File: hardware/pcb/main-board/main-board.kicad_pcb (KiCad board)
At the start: 2 copper layers, 100 x 80 mm, 44 parts, among them J1 USB-C, J10 CH552G_KEYBOARD_MCU, J11 KEYBOARD_BACKLIGHT_LEDS, J12 SPEAKER_1W_8OHM, J2 BATT_2x18650_PARALLEL, J3 BOOT0_OVERRIDE_JUMPER, J4 SWD_DEBUG, J5 MICROSD, J6 CR2032_HOLDER, J7 U.FL, J8 SMA_EDGE, J9 RA8875_DISPLAY_MODULE, Q1 2N7002, SW1 PWR_KEY, SW2 RESET, U1 MCP73831-2-OT, U10 PAM8403D, U2 IP5306, U3 AMS1117-3.3, U4 AMS1117-3.3, U5 GD32VF103CCT6, U6 W25Q64JVSSIQ, U7 23LC1024, U8 DS3231M, U9 ESP32-C3-MINI-1U, Y1 8MHz

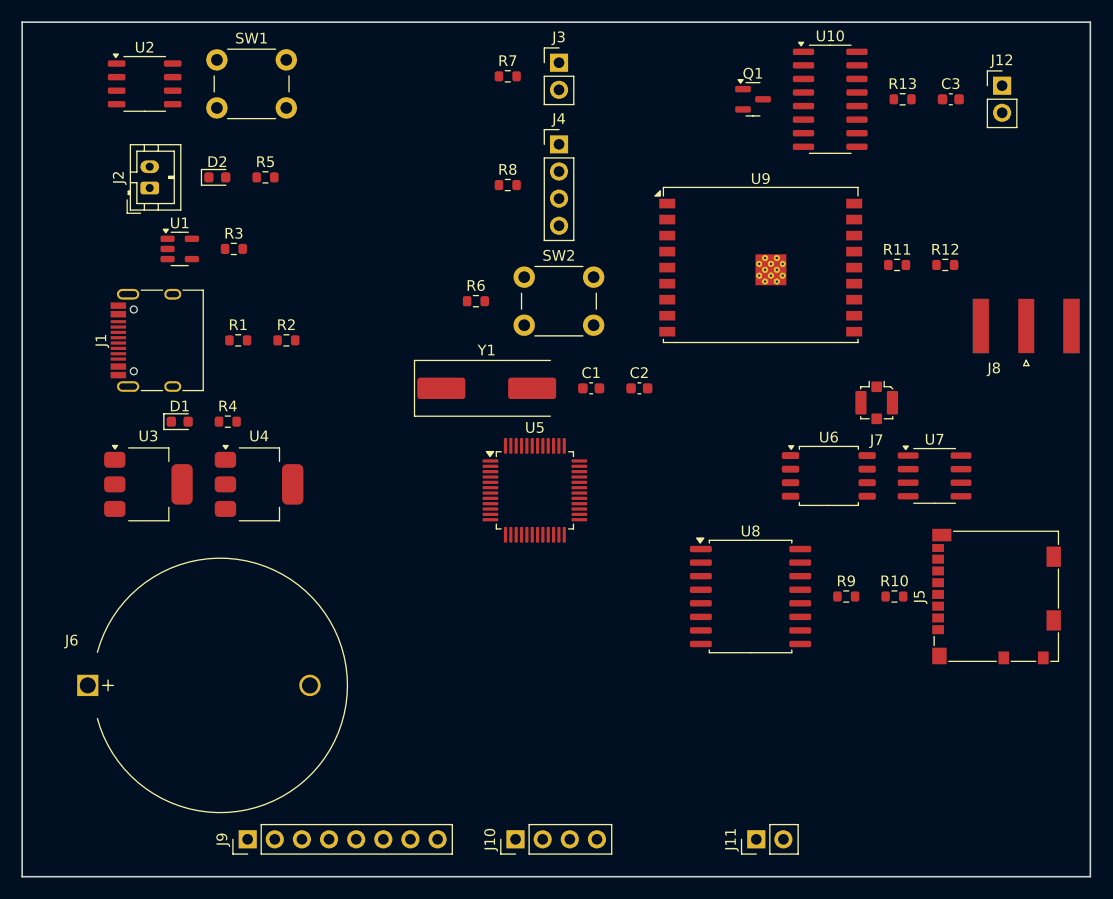
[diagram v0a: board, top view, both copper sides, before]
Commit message: hardware: route the Main Board PCB with Freerouting
Routes main-board.kicad_pcb (was placement-only) via Freerouting 2.2.4,
run headless through its CLI -- no GUI, no manual click-routing. Neither
Freerouting nor a Java runtime new enough to run it (it needs Java 25;
the environment had 21) were available, so both were fetched for this
pass.

170 of 171 connections auto-routed across 2 layers (F.Cu/B.Cu) in 10
passes (~31s). One net (/DISP_CS, MCU to the display header) is left
unrouted -- it sits in a congested area the autorouter couldn't clear
even at 30 passes, and finishing that one trace by hand in KiCad's PCB
editor is the realistic path forward, not more autorouter time.

kicad-cli pcb drc: 12 violations, all the same pre-existing
drill_out_of_range on U9's placeholder footprint (see prior commit) --
courtyard/shorting/clearance all clean.

Co-Authored-By: Claude Sonnet 5 <noreply@anthropic.com>
Claude-Session: https://claude.ai/code/session_01Qv22nN2Gzvn3yFBup6Askg
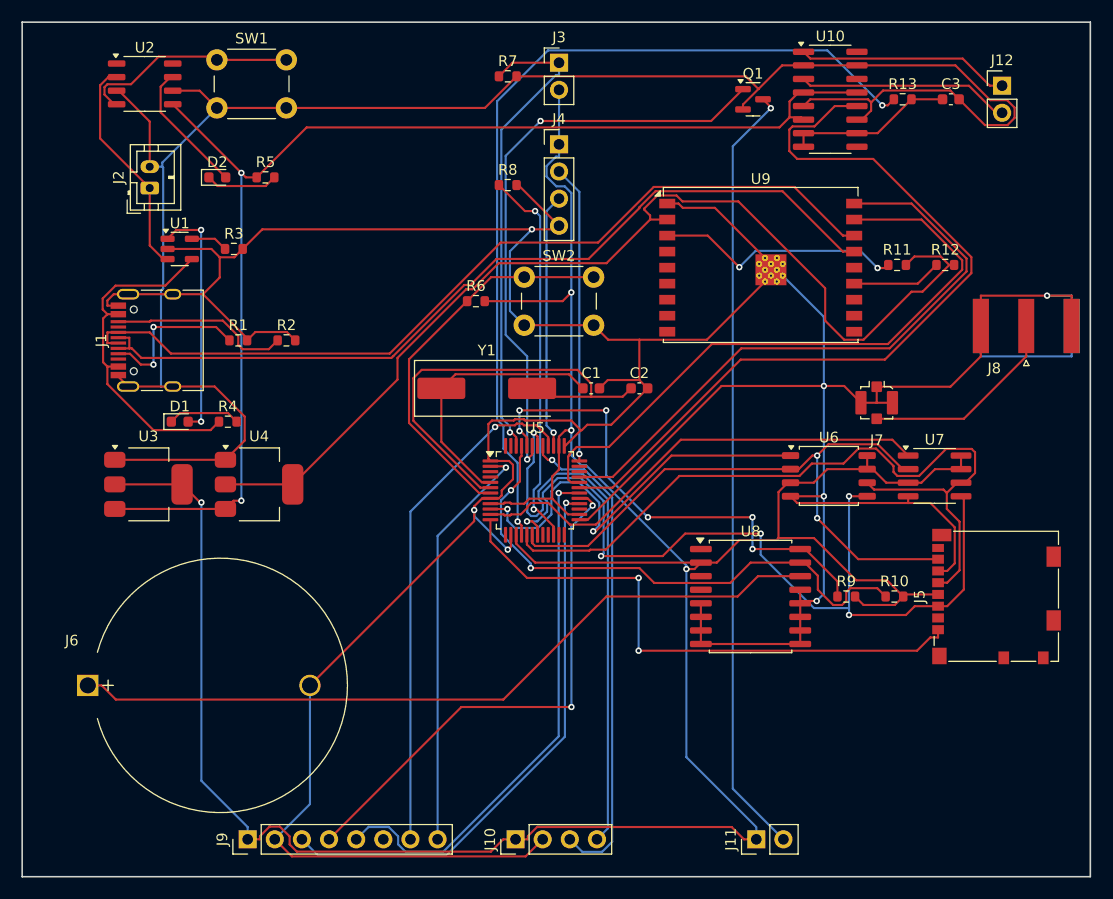
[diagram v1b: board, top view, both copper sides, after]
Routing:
- net GND: track 0.00 -> 582.2 mm, vias 0 -> 7
- net /+3V3_MCU: track 0.00 -> 275.2 mm, vias 0 -> 4
- net +5V: track 0.00 -> 115.3 mm, vias 0 -> 2
- net /+3V3_RF: track 0.00 -> 98.6 mm
- net /AUDIO_PWM: track 0.00 -> 83.0 mm, vias 0 -> 2
- net /USB_DP: track 0.00 -> 81.1 mm
- net /USB_DN: track 0.00 -> 80.1 mm
- net /SPI1_MOSI: track 0.00 -> 80.1 mm, vias 0 -> 5
- net /AUDIO_SHDN: track 0.00 -> 76.9 mm
- net /SPI1_SCK: track 0.00 -> 73.1 mm
- net /KBL_DRAIN: track 0.00 -> 73.0 mm, vias 0 -> 1
- net /VBAT_RTC: track 0.00 -> 72.0 mm
- net /USART1_TX: track 0.00 -> 60.1 mm
- net /SPI1_MISO: track 0.00 -> 59.8 mm, vias 0 -> 2
- net /USART1_RX: track 0.00 -> 58.1 mm
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
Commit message: hardware: regenerate the Main Board PCB against the corrected netlist
The previous PCB was routed against the pre-datasheet-fix netlist, so
its net-to-pad assignments on the MCU, ESP32-C3 module, and IP5306
were wrong, not just stale. Regenerated from scratch: fresh netlist
export, fresh placement (build_pcb.py), fresh Freerouting pass.

Freerouting completed 170 of 171 nets; the one holdout was /USB_DN
(J1's two D- pins, 1mm apart with /USB_DP's pad physically between
them) rather than /DISP_CS this time -- /DISP_CS routed cleanly once
it was routing the pad that's actually /DISP_CS now (pad 25, not the
old netlist's pad 27). Finished /USB_DN by hand: the west side of the
connector was already fully claimed by /USB_DP, VBUS, and /CHG_STAT
with no spare lane, so it routes east instead, into open board area.

Result: 171/171 routed, DRC clean except the pre-existing
drill_out_of_range warnings on U9's WROOM-02U placeholder footprint
(unrelated, already documented).

Co-Authored-By: Claude Sonnet 5 <noreply@anthropic.com>
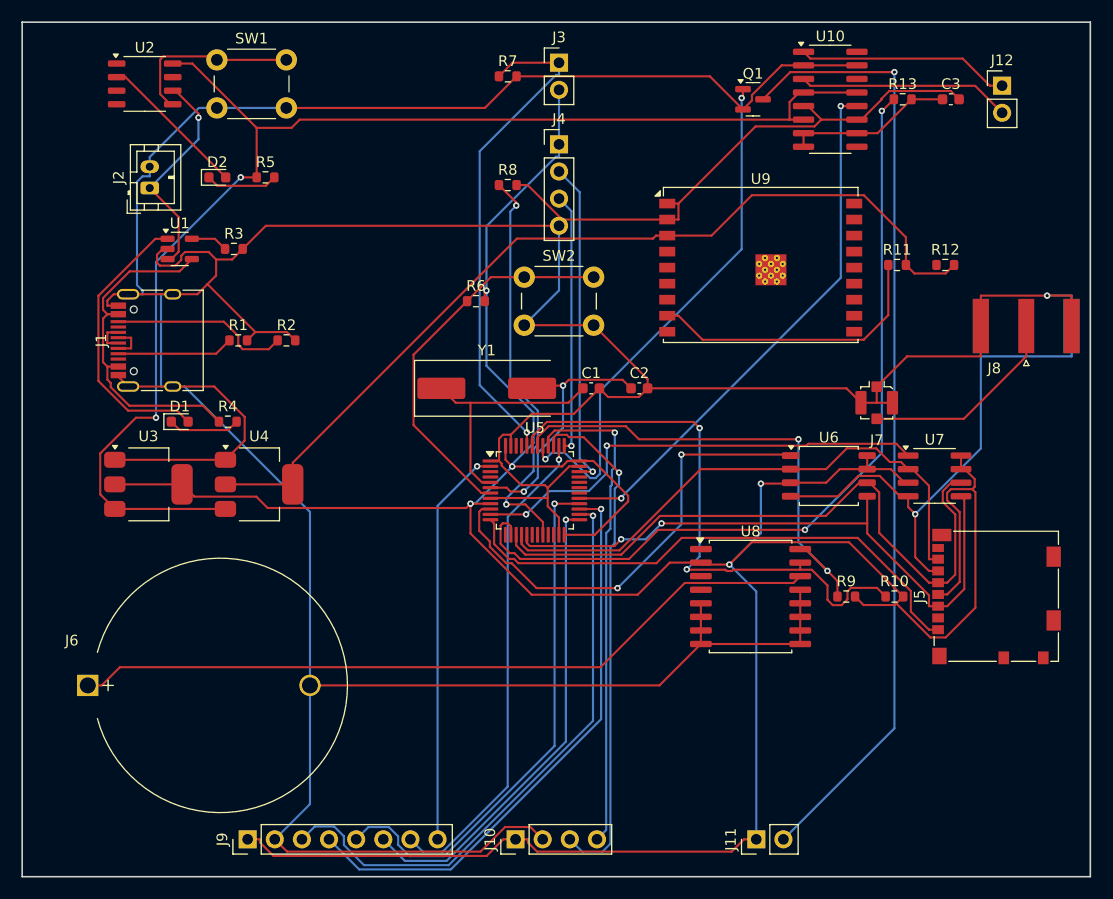
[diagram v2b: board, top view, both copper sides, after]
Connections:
- U2 pad 2: /VBATT -> /BATT_LED1
- U2 pad 3: GND -> unconnected-(U2-LED2-Pad3)
- U2 pad 4: /PWR_KEY -> unconnected-(U2-LED3-Pad4)
- U2 pad 5: +5V -> /PWR_KEY
- U2 pad 6: GND -> /VBATT
- U2 pad 7: /BATT_LED1 -> unconnected-(U2-SW-Pad7)
- U2 pad 8: unconnected-(U2-LED2-Pad8) -> +5V
- U5 pad 14: GND -> /AUDIO_PWM
- U5 pad 15: /+3V3_MCU -> /SPI1_SCK
- U5 pad 16: /AUDIO_PWM -> /SPI1_MISO
- U5 pad 17: /SPI1_SCK -> /SPI1_MOSI
- U5 pad 18: /SPI1_MISO -> unconnected-(U5-PB0-Pad18)
- U5 pad 19: /SPI1_MOSI -> unconnected-(U5-PB1-Pad19)
- U5 pad 20: unconnected-(U5-PB0-Pad20) -> /BOOT1
- U5 pad 22: /BOOT1 -> unconnected-(U5-PB11-Pad22)
- U5 pad 23: unconnected-(U5-PB10-Pad23) -> GND
- U5 pad 24: unconnected-(U5-PB11-Pad24) -> /+3V3_MCU
- U5 pad 25: GND -> /DISP_CS
- U5 pad 26: /+3V3_MCU -> /SPI2_SCK
- U5 pad 27: /DISP_CS -> /SPI2_MISO
- U5 pad 28: /SPI2_SCK -> /SPI2_MOSI
- U5 pad 29: /SPI2_MISO -> /AUDIO_SHDN
- U5 pad 30: /SPI2_MOSI -> /USART1_TX
- U5 pad 31: /AUDIO_SHDN -> /USART1_RX
- U5 pad 32: /USART1_TX -> unconnected-(U5-PA11-Pad32)
- U5 pad 33: /USART1_RX -> unconnected-(U5-PA12-Pad33)
- U5 pad 34: unconnected-(U5-PA11-Pad34) -> /SWDIO
- U5 pad 35: unconnected-(U5-PA12-Pad35) -> GND
- U5 pad 36: /SWDIO -> /+3V3_MCU
- U5 pad 37: GND -> /SWCLK
- U5 pad 38: /+3V3_MCU -> /DISP_RESET
- U5 pad 39: /SWCLK -> /USART2_TX
- U5 pad 40: /DISP_RESET -> /USART2_RX
- U5 pad 41: /USART2_TX -> /KBD_BACKLIGHT_PWM
- U5 pad 42: /USART2_RX -> /I2C1_SCL
- U5 pad 43: /KBD_BACKLIGHT_PWM -> /I2C1_SDA
- U5 pad 44: /I2C1_SCL -> /BOOT0
- U5 pad 45: /I2C1_SDA -> unconnected-(U5-PB8-Pad45)
- U5 pad 46: /BOOT0 -> unconnected-(U5-PB9-Pad46)
- U5 pad 47: unconnected-(U5-PB8-Pad47) -> GND
- U5 pad 48: unconnected-(U5-PB9-Pad48) -> /+3V3_MCU
- U9 pad 10: unconnected-(U9-IO6-Pad10) -> (no net)
- U9 pad 11: unconnected-(U9-IO7-Pad11) -> (no net)
- U9 pad 13: /ESP_IO9 -> unconnected-(U9-IO1-Pad13)
- U9 pad 14: unconnected-(U9-IO10-Pad14) -> (no net)
- U9 pad 15: /USB_DN -> (no net)
- U9 pad 16: /USB_DP -> unconnected-(U9-IO10-Pad16)
- U9 pad 17: /USART1_TX -> (no net)
- U9 pad 18: /USART1_RX -> unconnected-(U9-IO4-Pad18)
- U9 pad 19: GND -> unconnected-(U9-IO5-Pad19)
- U9 pad 2: /+3V3_RF -> GND
- U9 pad 3: /ESP_EN -> /+3V3_RF
- U9 pad 4: unconnected-(U9-IO0/BOOT_SEL-Pad4) -> (no net)
- U9 pad 7: unconnected-(U9-IO3-Pad7) -> (no net)
- U9 pad 8: unconnected-(U9-IO4-Pad8) -> /ESP_EN
- U9 pad 9: unconnected-(U9-IO5-Pad9) -> (no net)
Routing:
- net /USB_DP: track 81.1 -> 3.05 mm
- net /USB_DN: track 80.1 -> 3.39 mm
- net /USART1_TX: track 60.1 -> 0.00 mm
- net /USART1_RX: track 58.1 -> 0.00 mm
- net /DISP_CS: track 0.00 -> 44.6 mm, vias 0 -> 1
- net /+3V3_MCU: track 275.2 -> 301.9 mm, vias 4 -> 5
- net /AUDIO_SHDN: track 76.9 -> 50.7 mm, vias 0 -> 2
- net GND: track 582.2 -> 557.4 mm, vias 7 -> 2
- net /SPI1_MOSI: track 80.1 -> 59.1 mm, vias 5 -> 2
- net /OSC_OUT: track 42.4 -> 24.7 mm, vias 0 -> 2
- net /KBL_DRAIN: track 73.0 -> 89.5 mm
- net /+3V3_RF: track 98.6 -> 85.5 mm
- net /SPI1_SCK: track 73.1 -> 62.0 mm
- net unconnected-(U9-IO5-Pad19): track 0.00 -> 11.0 mm
- net +5V: track 115.3 -> 124.8 mm
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
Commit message: hardware: add the IP5306's missing boost inductor
Datasheet verification (previous commit) found the IP5306's SW pin
(the boost converter's switch node) was wired to nothing -- the boost
path (BAT -> VOUT) couldn't function without an inductor there, and
none existed anywhere in this design.

Fixed per the IP5306 datasheet's own "Typical Application Schematic"
(Figure 7): a 1uH inductor (L1) bridges SW to BAT directly, not to
VOUT as an earlier read of this design assumed -- it's shared between
the buck charger and boost discharger. Added the reference circuit's
RC snubber (R14 0.5R + C4 22uF) on the SW node and a VOUT decoupling
cap (C5, simplified from the datasheet's 4-cap bank to one).

Regenerated the schematic (ERC clean) and the PCB from scratch against
the updated netlist: fresh placement (the new parts go in the open
board area below the MCU cluster, since the CR2032 holder's real
courtyard already fills the power-tree column), fresh Freerouting
pass, one net (/USB_DN, unrelated -- same fix as the previous PCB
regeneration) finished by hand. All 87 nets routed, DRC clean except
the pre-existing, already-documented ESP32 placeholder footprint
warning.

Flagged for the next design-review pass: the new SW/inductor path
carries boost-converter current (up to 2.4A) but was auto-routed at
the board's default 0.2mm trace width, which is undersized for it.

Co-Authored-By: Claude Sonnet 5 <noreply@anthropic.com>
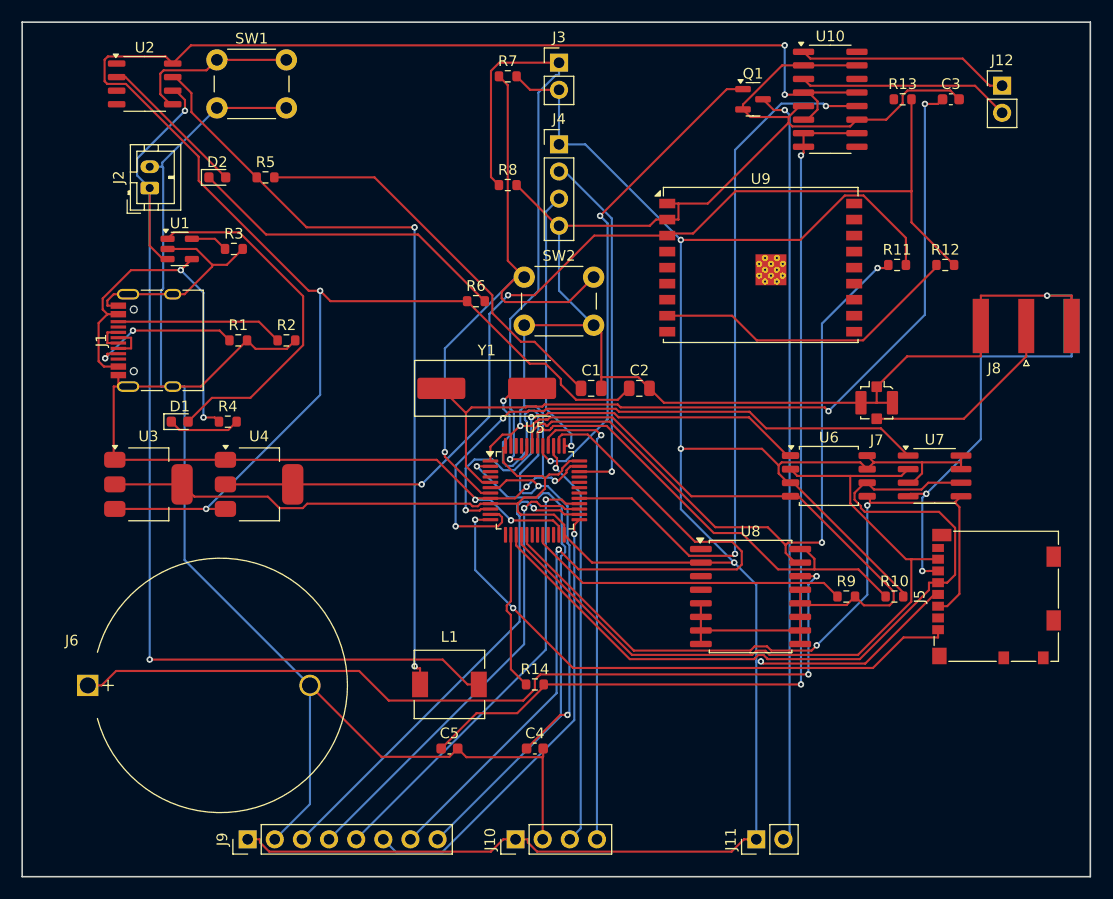
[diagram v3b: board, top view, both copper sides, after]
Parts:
- added C4: 20pF, C_0603_1608Metric, F.Cu at (48.0, 68.0)
- added C5: 100nF, C_0603_1608Metric, F.Cu at (40.0, 68.0)
- added L1: 1uH, L_6.3x6.3_H3, F.Cu at (40.0, 62.0)
- added R14: 1k, R_0603_1608Metric, F.Cu at (48.0, 62.0)
- C1, C2: value 20pF -> 22uF; footprint C_0603_1608Metric -> C_0805_2012Metric
- C3: value 100nF -> 20pF
- R11: value 10k -> 4.7k
- R13: value 1k -> 10k
- R5: value 1k -> 0.5R
- R6: value 10k -> 1k
- R9: value 4.7k -> 10k
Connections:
- C1 pad 1: /OSC_IN -> /SNUBBER_MID
- C2 pad 1: /OSC_OUT -> +5V
- C3 pad 1: /AUDIO_IN -> /OSC_IN
- R10 pad 1: /I2C1_SDA -> /I2C1_SCL
- R11 pad 1: /ESP_EN -> /I2C1_SDA
- R11 pad 2: /+3V3_RF -> /+3V3_MCU
- R12 pad 1: /ESP_IO9 -> /ESP_EN
- R13 pad 1: /AUDIO_PWM -> /ESP_IO9
- R13 pad 2: /AUDIO_IN -> /+3V3_RF
- R5 pad 1: +5V -> /IP5306_SW
- R5 pad 2: /BATT_LED1_R -> /SNUBBER_MID
- R6 pad 1: /NRST -> +5V
- R6 pad 2: /+3V3_MCU -> /BATT_LED1_R
- R7 pad 1: /BOOT0 -> /NRST
- R7 pad 2: GND -> /+3V3_MCU
- R8 pad 1: /BOOT1 -> /BOOT0
- R9 pad 1: /I2C1_SCL -> /BOOT1
- R9 pad 2: /+3V3_MCU -> GND
- U2 pad 7: unconnected-(U2-SW-Pad7) -> /IP5306_SW
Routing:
- net /AUDIO_IN: track 15.6 -> 93.0 mm, vias 0 -> 2
- net /VBATT: track 20.6 -> 95.6 mm, vias 1 -> 2
- net /IP5306_SW: track 0.00 -> 72.7 mm, vias 0 -> 2
- net /AUDIO_PWM: track 77.7 -> 14.9 mm, vias 2 -> 0
- net /OSC_IN: track 23.1 -> 80.0 mm, vias 0 -> 2
- net +5V: track 124.8 -> 181.2 mm, vias 2 -> 4
- net GND: track 557.4 -> 517.8 mm, vias 2 -> 8
- net /SNUBBER_MID: track 0.00 -> 37.9 mm
- net /OSC_OUT: track 24.7 -> 60.7 mm, vias 2 -> 3
- net /DISP_RESET: track 46.0 -> 74.8 mm
- net /BATT_LED1_R: track 6.78 -> 30.6 mm
- net /NRST: track 36.3 -> 58.6 mm, vias 0 -> 1
- net /SPI1_MISO: track 52.4 -> 72.5 mm
- net /KBL_DRAIN: track 89.5 -> 71.2 mm
- net /AUDIO_SHDN: track 50.7 -> 68.0 mm
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
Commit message: hardware: replace the ESP32-C3-MINI-1U placeholder with its real footprint
The datasheet verification pass (two commits back) fixed the schematic
symbol's pin numbers but left the PCB footprint as the same-family
RF_Module:ESP32-C3-WROOM-02U placeholder. Rather than hand-transcribe
a 53-pad castellated land pattern off the datasheet's dimension
drawing -- error-prone, and exactly the kind of mistake this whole
verification effort exists to catch -- vendored the real footprint
from Espressif's official KiCad library (CC-BY-SA 4.0, same terms as
KiCad's own libraries) into a new gridnet_footprints.pretty/, with
build_pcb.py gaining a small local-footprint-library lookup to load
it. Verified before use: 53 distinct pad numbers, pad 49 (GND) present
as the expected 3x3 thermal-via array, matching the datasheet table
the symbol's pins were already checked against.

Regenerated the schematic (ERC clean) and the PCB from scratch:
placement, Freerouting pass, one net (/USB_DN, same unrelated fix as
the last two PCB regenerations) finished by hand. Result: 0 DRC
violations, 0 unconnected items -- the drill_out_of_range warnings
present in every DRC run so far in this project's history are gone,
since they traced entirely to the placeholder's own hole spec.

New finding, not yet addressed: the real footprint has ~34 more GND/NC
pads than the schematic symbol wires, including a 3x3 thermal-pad via
array under pin 49 that isn't stitched to any ground pour. Espressif's
guidance recommends grounding all of them for RF/thermal performance;
flagged in the PCB README as a follow-up, not fixed in this pass.

Co-Authored-By: Claude Sonnet 5 <noreply@anthropic.com>
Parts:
- U9: footprint ESP32-C3-WROOM-02U -> ESP32-C3-MINI-1U
- moved U9 0.30 mm to (69.1, 22.7)
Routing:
- net /USB_DP: track 3.05 -> 76.5 mm, vias 0 -> 2
- net /USB_DN: track 3.39 -> 73.9 mm
- net GND: track 517.8 -> 576.5 mm, vias 8 -> 3
- net /USART1_TX: track 0.00 -> 45.9 mm, vias 0 -> 2
- net /USART1_RX: track 0.00 -> 38.7 mm
- net +5V: track 181.2 -> 145.3 mm
- net /DISP_RESET: track 74.8 -> 44.8 mm
- net /ESP_IO9: track 0.00 -> 24.6 mm, vias 0 -> 2
- net /SPI1_MISO: track 72.5 -> 52.5 mm
- net /OSC_IN: track 80.0 -> 96.6 mm, vias 2 -> 3
- net /SPI2_MISO: track 44.3 -> 60.6 mm
- net /SRAM_CS: track 58.3 -> 43.0 mm
- net /OSC_OUT: track 60.7 -> 45.6 mm, vias 3 -> 2
- net /+3V3_MCU: track 306.9 -> 293.4 mm, vias 4 -> 7
- net /SPI2_MOSI: track 42.5 -> 55.8 mm
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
